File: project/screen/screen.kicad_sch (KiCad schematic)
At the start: 34 parts, among them J1 Conn_01x12_Female, J2 Conn_01x06_Female, J3 USB_C_Receptacle_USB2.0, J4 Conn_01x02_Female, SW1 SW_DPDT_x2, SW2 SW_Push, SW3 SW_Push, U1 SPX3819M5-L-3-3, U2 ESP-12E, U3 TP4056_[C16581]

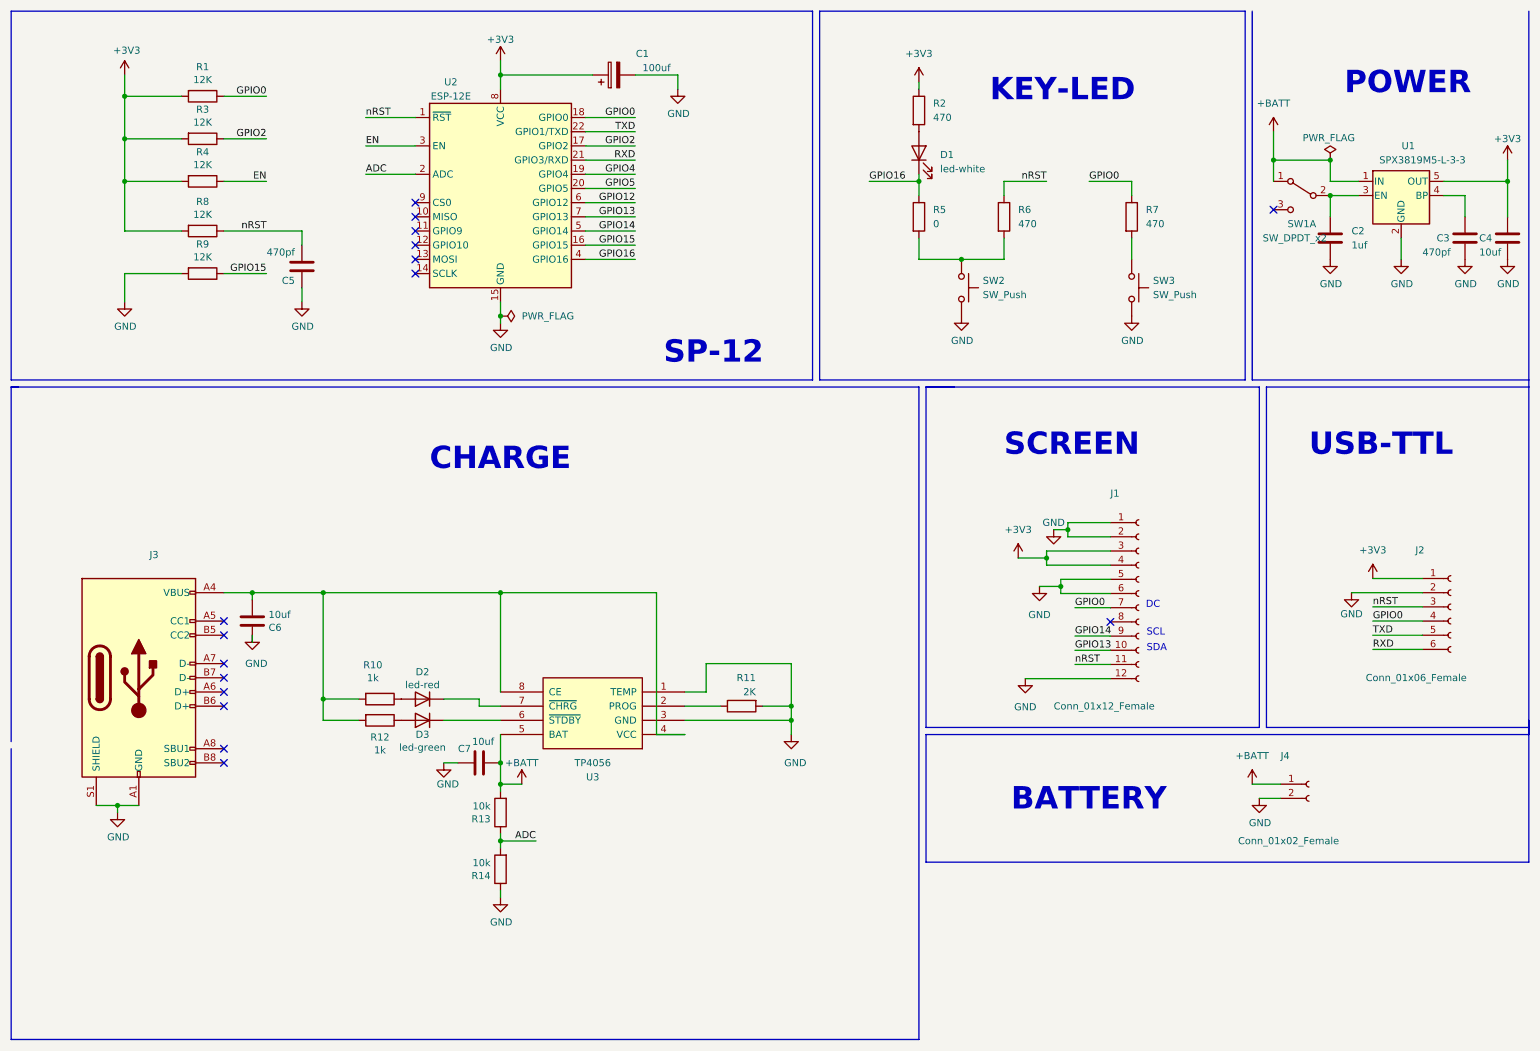
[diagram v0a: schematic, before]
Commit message: feat:add screen 0.96 project
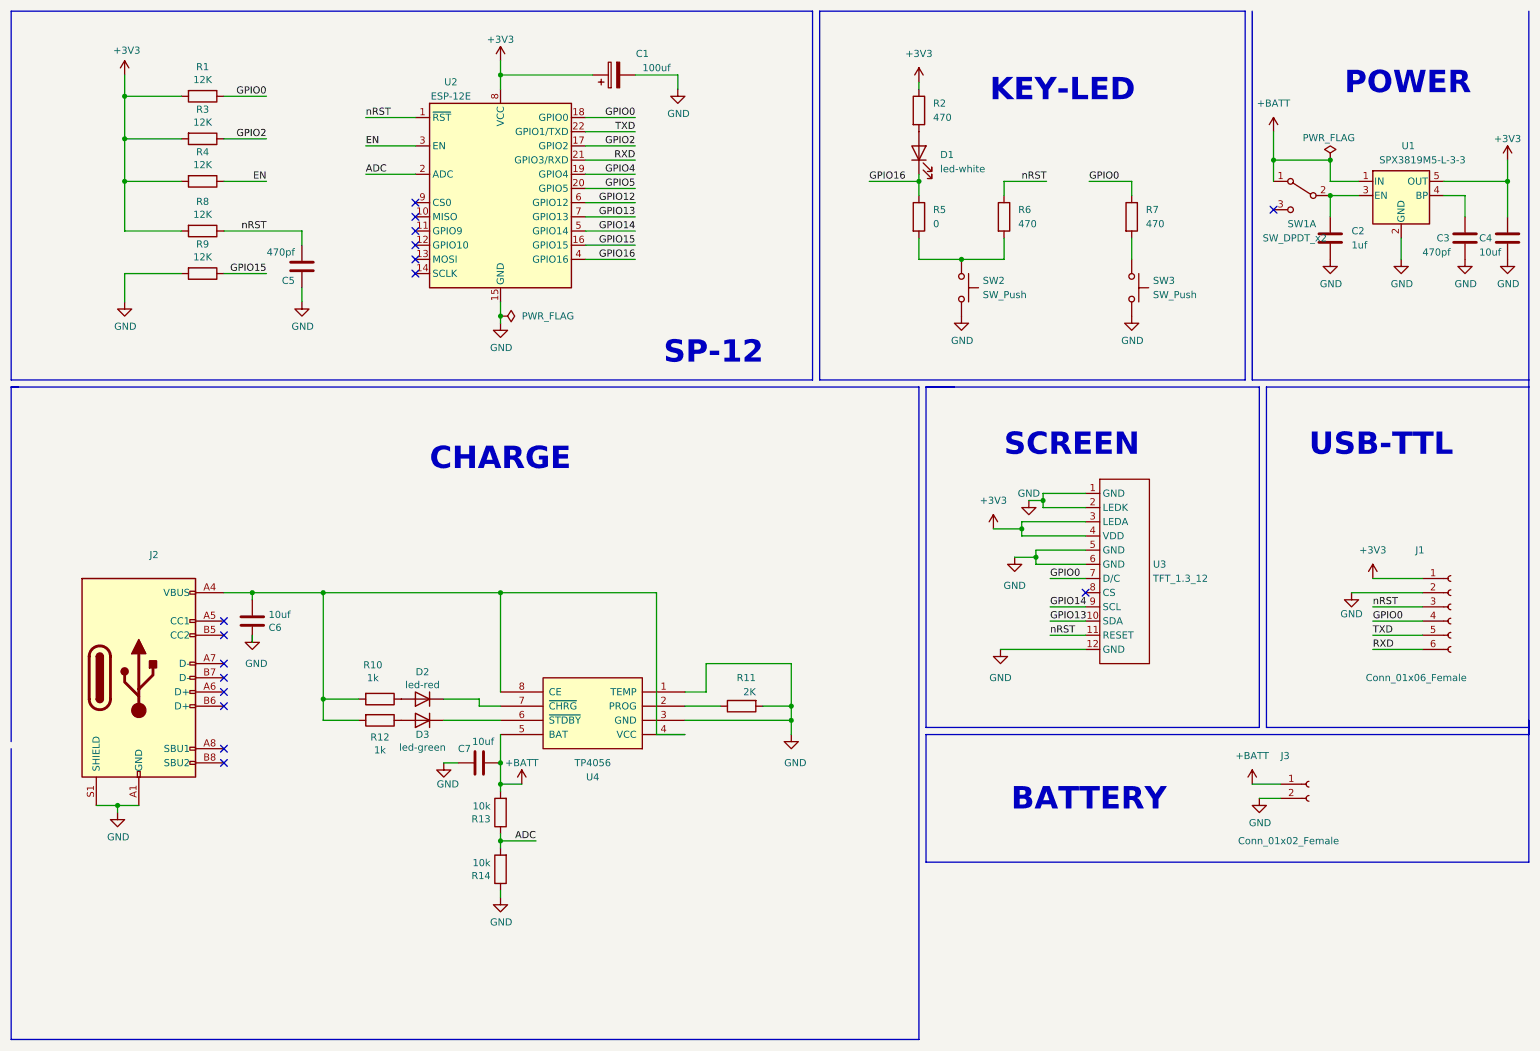
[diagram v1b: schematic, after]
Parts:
- removed J1: Conn_01x12_Female, My-lib:TFT_1.4_12_front, symbol Connector:Conn_01x12_Female
- added U3: TFT_1.3_12, My-lib-footprints:TFT_1.3_12_front, symbol My-lib:TFT_1.3_12
- renumbered J2 to J1, J3 to J2, J4 to J3, U3 to U4
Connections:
- net +3V3: now also U3.3 (LEDA), U3.4 (VDD)
- net GND: now also U3.1 (GND), U3.12 (GND), U3.2 (LEDK), U3.5 (GND), U3.6 (GND)
- net GPIO0: now also U3.7 (D/C)
- net GPIO13: now also U3.10 (SDA)
- net GPIO14: now also U3.9 (SCL)
- net nRST: now also U3.11 (RESET)
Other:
- note removed: "DC"
- note removed: "SCL"
- note removed: "SDA"
